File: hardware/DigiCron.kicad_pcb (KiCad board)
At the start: 2 copper layers, 36 x 36 mm, 28 parts, among them J100 Solder pad, J101 Solder pad, J102 Solder pad, J103 Solder pad, J200 Conn_Receptacle_2P, Q200 AO3401A, U100 MDBT50Q-U1MV2, U101 HCMS-3917, U102 HCMS-3917, U103 LTR-390UV-01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

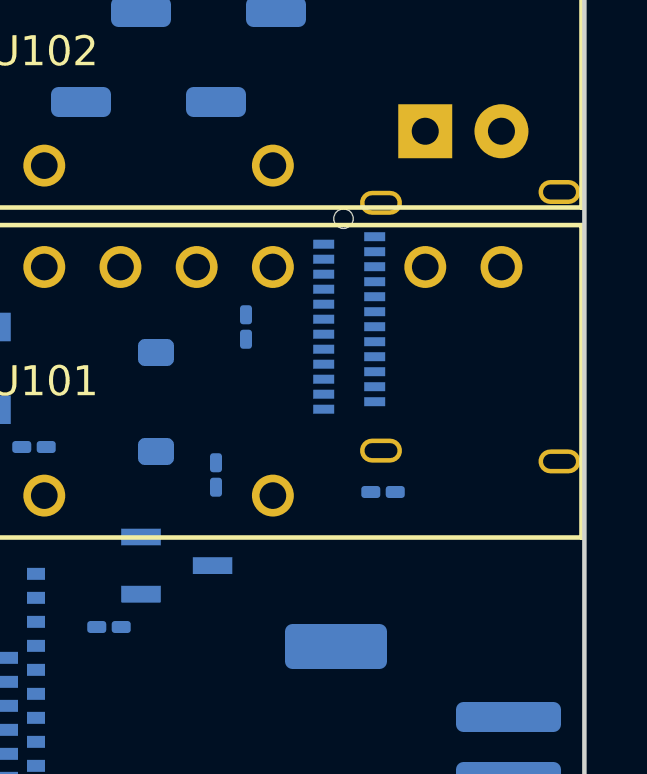
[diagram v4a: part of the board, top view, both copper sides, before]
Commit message: Reposition USB port on board
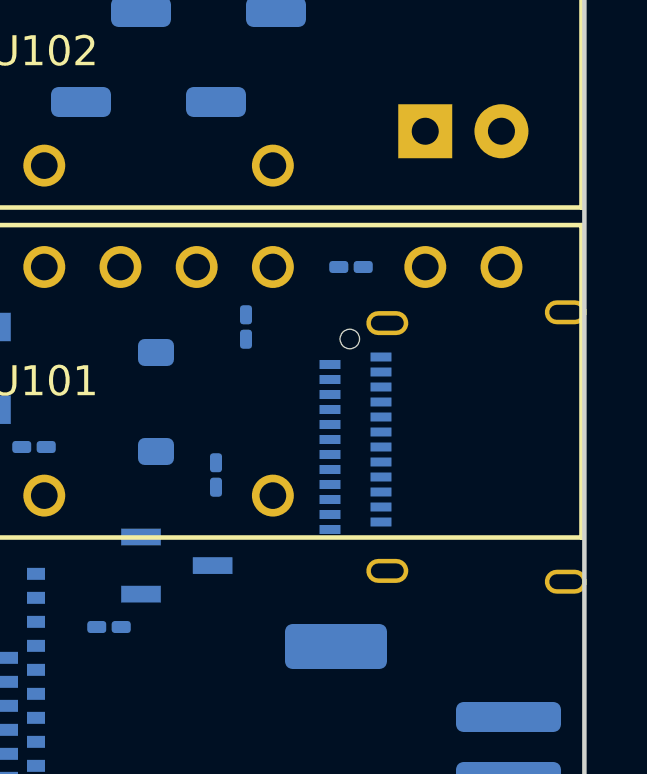
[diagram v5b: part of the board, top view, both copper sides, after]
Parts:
- moved R201 7.58 mm to (208.1, 81.5)
- moved X200 4.02 mm to (208.1, 87.5)
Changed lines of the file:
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@@
 		(tags "AO3401A ")
 		(property "Reference" "Q200"
-			(at -0.5475 4.3062 0)
+			(at -3.0475 0.8062 0)
 			(unlocked yes)
 			(layer "B.SilkS")
@@
 			(net 0)
 			(net_name "")
-			(layers "*.Cu")
+			(layers "F&B.Cu")
 			(hatch full 0.508)
 			(connect_pads
@@
 		(tags "resistor handsolder")
 		(property "Reference" "R202"
-			(at -1.0675 -1.5 0)
+			(at 0.4325 -2.5 -90)
 			(layer "B.SilkS")
 			(effects
@@
 		(tags "connector JST PH horizontal")
 		(property "Reference" "J200"
-			(at 5.5 3.1 0)
+			(at 0 -5.9 -90)
 			(layer "B.SilkS")
 			(effects
@@
 	(footprint "Resistor_SMD:R_0201_0603Metric_Pad0.64x0.40mm_HandSolder"
 		(layer "B.Cu")
-		(at 209.1875 89.04 180)
+		(at 208.12 81.54 180)
 		(descr "Resistor SMD 0201 (0603 Metric), square (rectangular) end terminal, IPC_7351 nominal with elongated pad for handsoldering. (Body size source: https://www.vishay.com/docs/20052/crcw0201e3.pdf), generated with kicad-footprint-generator")
 		(tags "resistor handsolder")
 		(property "Reference" "R201"
-			(at 0.0675 -1.5 0)
+			(at 0.0675 1 0)
 			(layer "B.SilkS")
 			(effects
@@
 	(footprint "USB-C:12401598E4#2A"
 		(layer "B.Cu")
-		(at 207.87 83.53 -90)
+		(at 208.08 87.54 -90)
 		(property "Reference" "X200"
-			(at 5.51 -4.75 0)
+			(at -7 -7.04 -90)
 			(layer "B.SilkS")
 			(effects

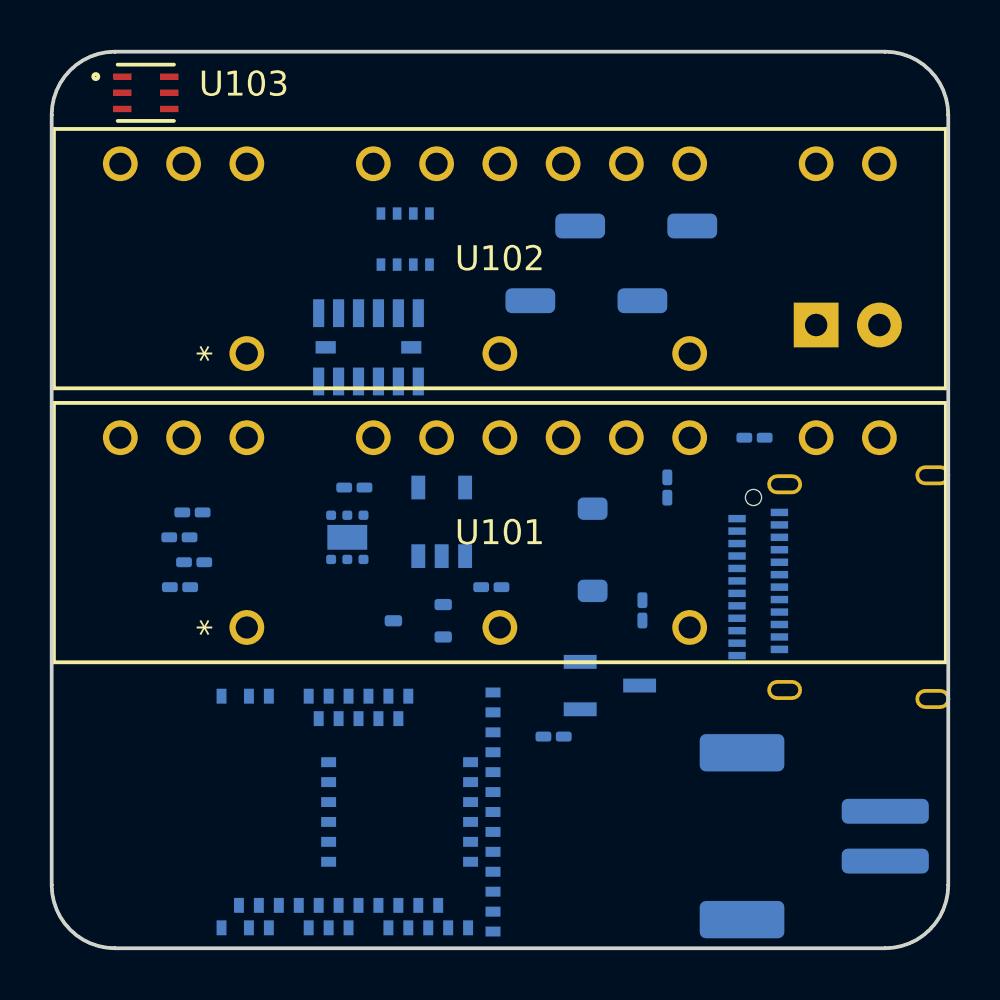
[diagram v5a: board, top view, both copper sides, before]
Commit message: Improve power sources for IR LED, vibration motor and piezo buzzer
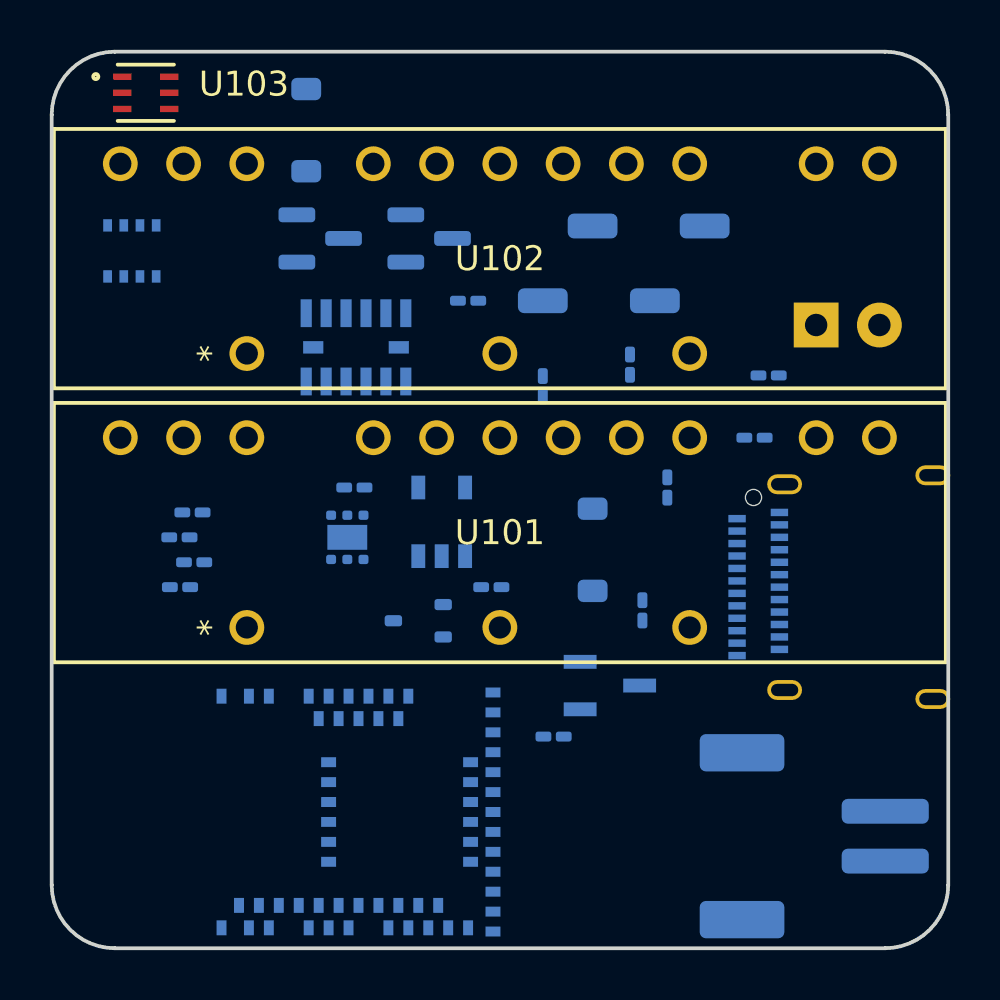
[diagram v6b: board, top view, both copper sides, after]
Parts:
- added D101: 1N4148W, Diode_SMD:D_SOD-123, B.Cu at (190.1, 69.2)
- added Q101: BSS138, Package_TO_SOT_SMD:SOT-23, B.Cu at (195.1, 73.5)
- added Q102: AO3400A, Package_TO_SOT_SMD:SOT-23, B.Cu at (190.7, 73.5)
- added R101: 18, Capacitor_SMD:C_0201_0603Metric_Pad0.64x0.40mm_HandSolder, B.Cu at (208.7, 79.0)
- added R102: 100, Capacitor_SMD:C_0201_0603Metric_Pad0.64x0.40mm_HandSolder, B.Cu at (199.6, 79.5)
- added R103: 10K, Capacitor_SMD:C_0201_0603Metric_Pad0.64x0.40mm_HandSolder, B.Cu at (196.6, 76.0)
- added R104: 100, Capacitor_SMD:C_0201_0603Metric_Pad0.64x0.40mm_HandSolder, B.Cu at (203.1, 78.6)
- moved U105 11.0 mm to (183.1, 74.0)
- moved U104 0.50 mm to (192.1, 77.9)
- moved J100 0.50 mm to (206.1, 73.0)
- moved J101 0.50 mm to (204.1, 76.0)
- moved J102 0.50 mm to (201.6, 73.0)
- moved J103 0.50 mm to (199.6, 76.0)
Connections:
- net PIEZO renamed PIEZO_B
- D100 pad 1: unconnected-(D100-K-Pad1) -> Net-(D100-K)
- D100 pad 2: unconnected-(D100-A-Pad2) -> +5V
- J100 pad 1: GND -> Net-(D101-A)
- J101 pad 1: VIBMOTOR -> +3V3
- J102 pad 1: GND -> PIEZO_A
- U100 pad 11: VIBMOTOR -> PIEZO_A
- U100 pad 20: A0 -> VIBMOTOR
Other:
- board text added: "PA"
- board text added: "PB"
- board text removed: "P+"
- board text removed: "P-"

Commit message: Add voltage divider and replace boost converter
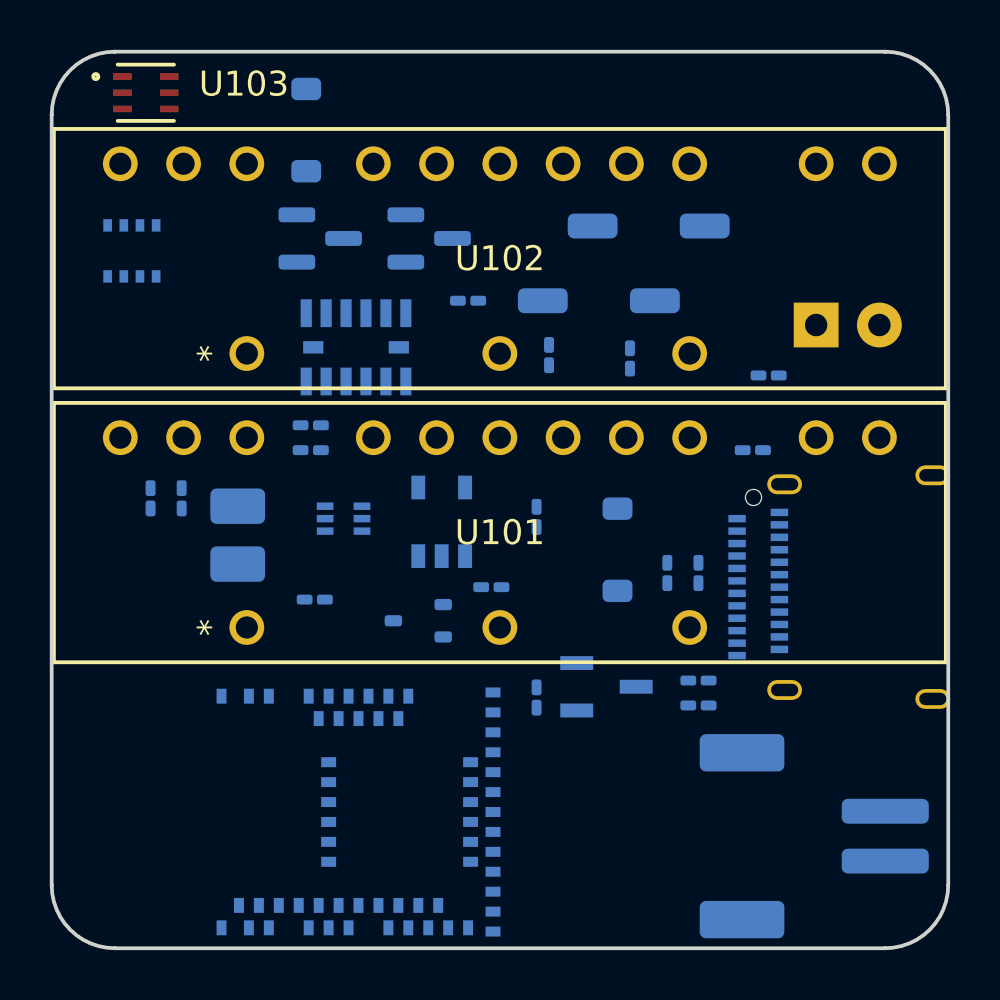
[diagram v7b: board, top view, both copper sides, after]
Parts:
- added R204: 732K, Resistor_SMD:R_0201_0603Metric_Pad0.64x0.40mm_HandSolder, B.Cu at (190.3, 82.0)
- added R205: 732K, Resistor_SMD:R_0201_0603Metric_Pad0.64x0.40mm_HandSolder, B.Cu at (190.3, 81.0)
- added R206: 100K, Resistor_SMD:R_0201_0603Metric_Pad0.64x0.40mm_HandSolder, B.Cu at (205.9, 91.3)
- added R207: 100K, Resistor_SMD:R_0201_0603Metric_Pad0.64x0.40mm_HandSolder, B.Cu at (205.9, 92.3)
- C202, C203, C204: value 10u -> 22u
- L200: value 2.2u -> 1u; footprint Inductor_SMD:L_0201_0603Metric_Pad0.64x0.40mm_HandSolder -> Inductor_SMD:L_1008_2520Metric_Pad1.43x2.20mm_HandSolder
- R100: renamed from R101; value 18 -> 30
- U201: value TPS610997DRV -> TPS61023DRLR; footprint Package_SON:WSON-6-1EP_2x2mm_P0.65mm_EP1x1.6mm -> TPS61023:DRL0006A
- moved C201 13.8 mm to (199.4, 84.7), turned to -90 degrees
- moved C202 5.98 mm to (190.5, 88.0)
- moved L200 5.06 mm to (187.4, 85.5), turned to 90 degrees
- moved R200 3.65 mm to (205.9, 87.0)
- moved C204 3.57 mm to (185.1, 84.0), turned to -90 degrees
- moved C203 3.11 mm to (183.9, 84.0), turned to -90 degrees
- moved C200 1.80 mm to (204.6, 87.0)
- moved R202 1.71 mm to (199.4, 92.0), turned to 90 degrees
- moved R101 1.27 mm to (199.9, 78.2)
- moved D200 1.00 mm to (202.6, 86.0)
- moved U201 0.76 mm to (191.6, 84.8), turned to 180 degrees
- moved R201 0.50 mm to (208.1, 82.0)
- moved R103 0.25 mm to (203.1, 78.4)
- moved Q200 0.15 mm to (202.2, 91.5)
- renumbered Q101 to Q100, Q102 to Q101, R102 to R101, R103 to R102, R104 to R103
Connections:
- U201 pad 1: GND -> Net-(U201-FB)
- U201 pad 2: Net-(U201-VOUT) -> 5V_EN
- U201 pad 3: GND -> VBAT
- U201 pad 4: 5V_EN -> GND
- U201 pad 6: VBAT -> Net-(U201-VOUT)

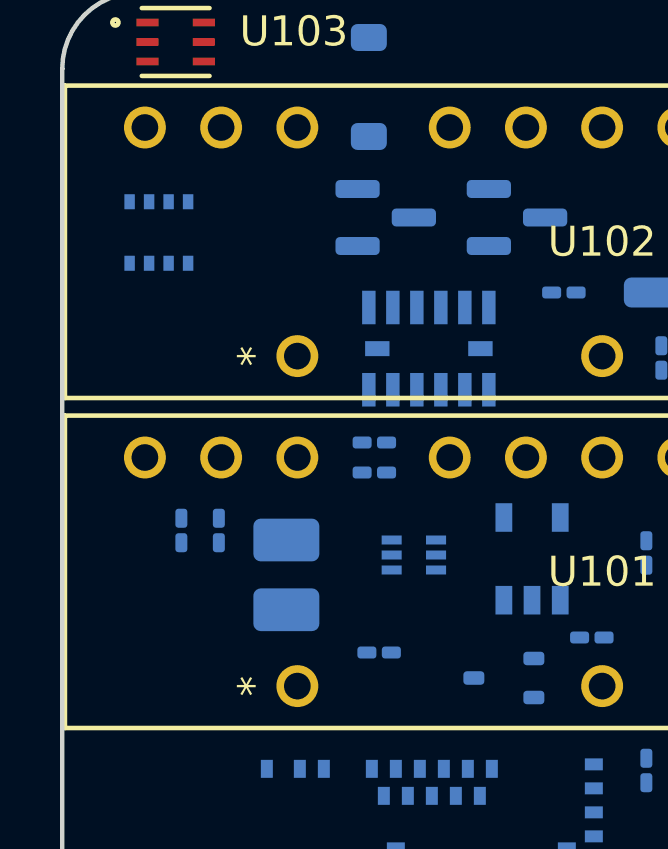
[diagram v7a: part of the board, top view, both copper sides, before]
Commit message: Add battery charging circuit
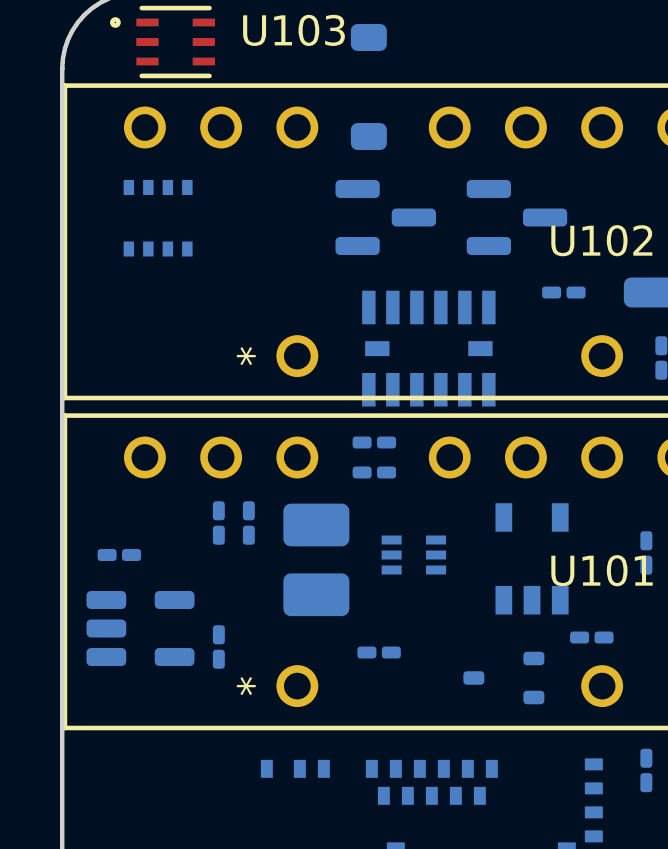
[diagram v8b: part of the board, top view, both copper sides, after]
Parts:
- added C205: 10u, Capacitor_SMD:C_0201_0603Metric_Pad0.64x0.40mm_HandSolder, B.Cu at (181.8, 84.8)
- added R208: 4.7K, Resistor_SMD:R_0201_0603Metric_Pad0.64x0.40mm_HandSolder, B.Cu at (185.1, 87.9)
- added U202: MCP73831-2-OT, Package_TO_SOT_SMD:SOT-23-5, B.Cu at (182.5, 87.2)
- moved C203 1.27 mm to (185.1, 83.7)
- moved L200 1.12 mm to (188.4, 85.0)
- moved C204 1.03 mm to (186.1, 83.7)
- moved U105 0.48 mm to (183.1, 73.6)
